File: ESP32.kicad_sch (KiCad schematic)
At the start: 5 parts, among them U1 ESP32-S3-WROOM-1

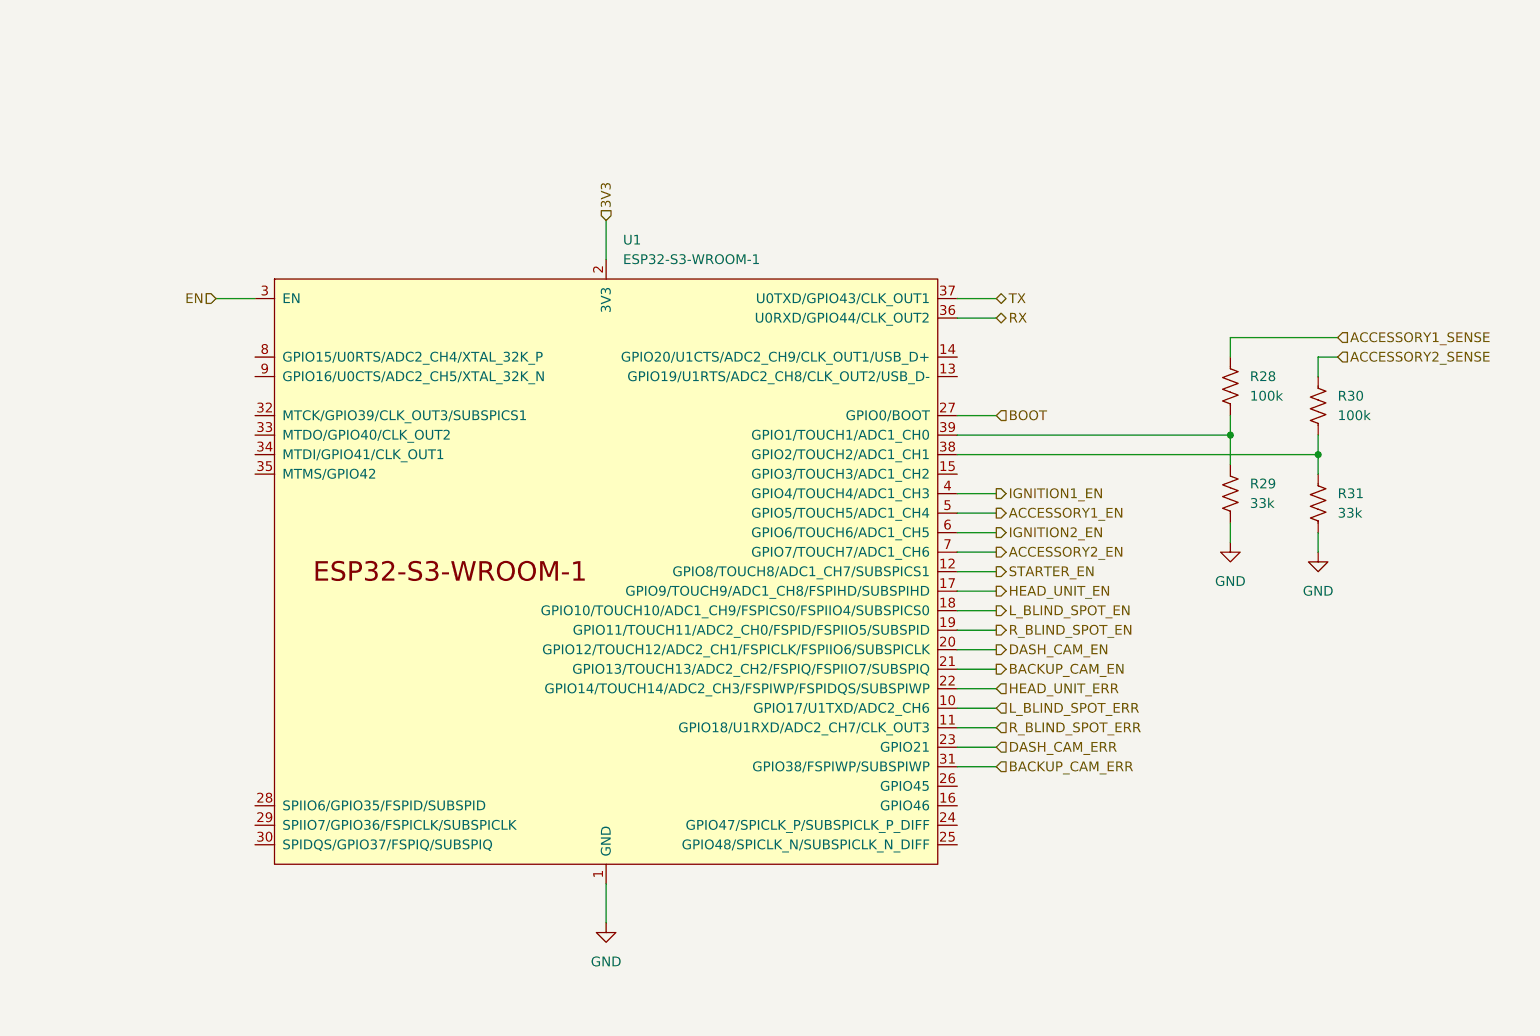
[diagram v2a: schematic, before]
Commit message: switch Ignition page to use load drivers rather than discrete FETs
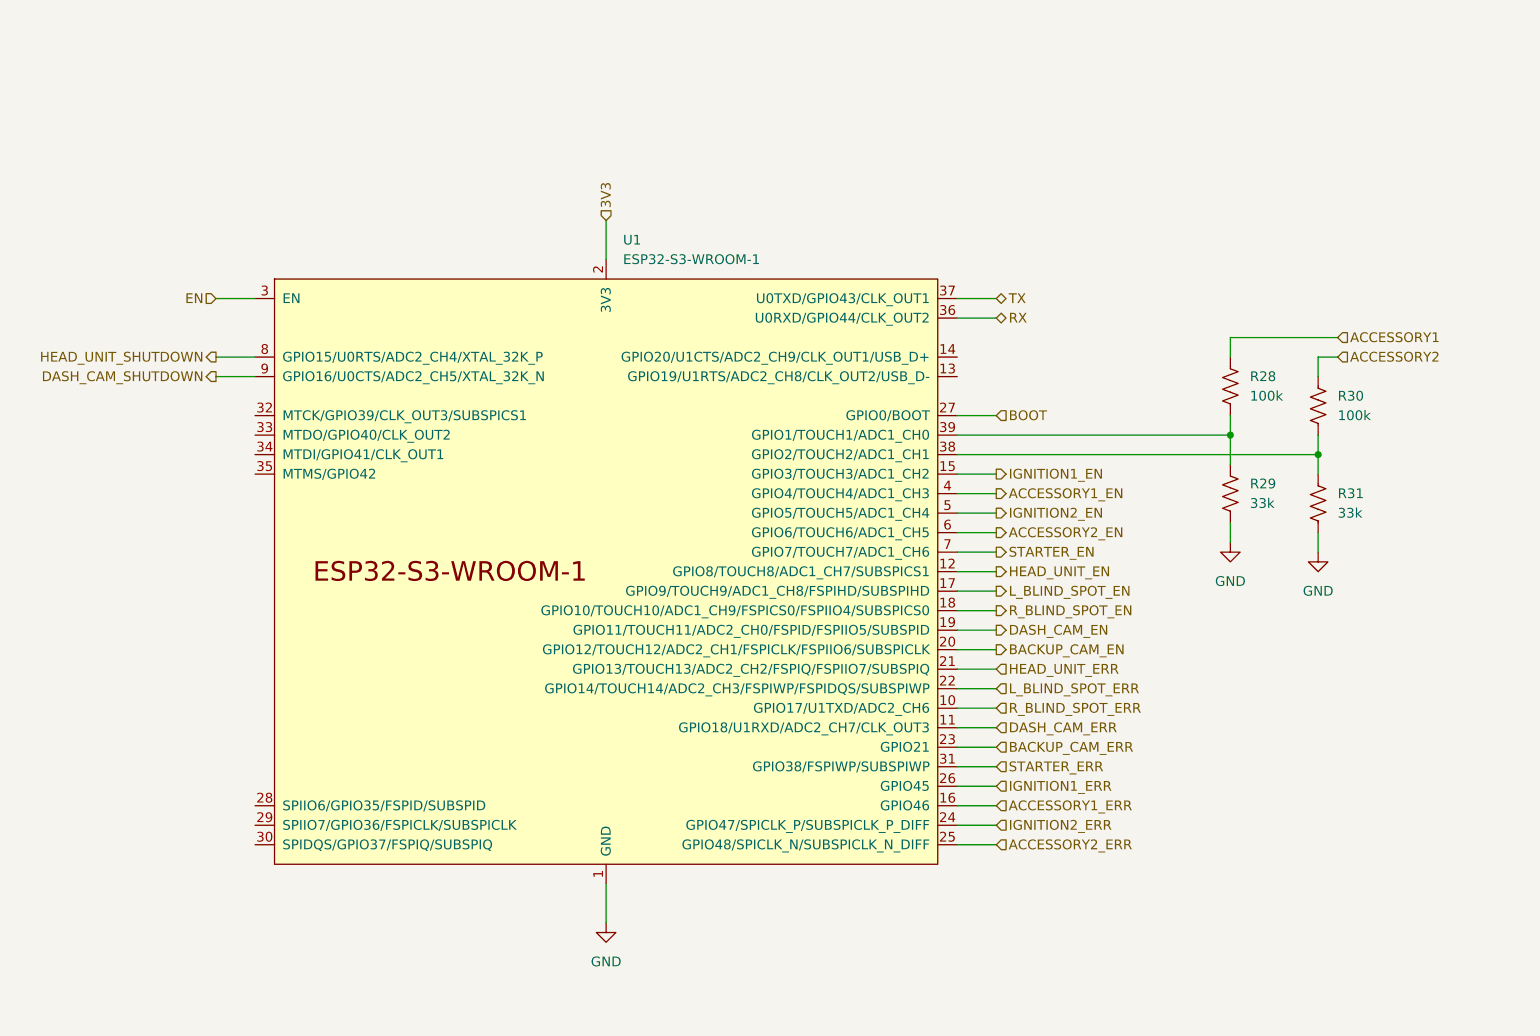
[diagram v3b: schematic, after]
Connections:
- net ACCESSORY1_EN: now also U1.4 (GPIO4/TOUCH4/ADC1_CH3); no longer U1.5 (GPIO5/TOUCH5/ADC1_CH4)
- net ACCESSORY2_EN: now also U1.6 (GPIO6/TOUCH6/ADC1_CH5); no longer U1.7 (GPIO7/TOUCH7/ADC1_CH6)
- net BACKUP_CAM_EN: now also U1.20 (GPIO12/TOUCH12/ADC2_CH1/FSPICLK/FSPIIO6/SUBSPICLK); no longer U1.21 (GPIO13/TOUCH13/ADC2_CH2/FSPIQ/FSPIIO7/SUBSPIQ)
- net BACKUP_CAM_ERR: now also U1.23 (GPIO21); no longer U1.31 (GPIO38/FSPIWP/SUBSPIWP)
- net DASH_CAM_EN: now also U1.19 (GPIO11/TOUCH11/ADC2_CH0/FSPID/FSPIIO5/SUBSPID); no longer U1.20 (GPIO12/TOUCH12/ADC2_CH1/FSPICLK/FSPIIO6/SUBSPICLK)
- net DASH_CAM_ERR: now also U1.11 (GPIO18/U1RXD/ADC2_CH7/CLK_OUT3); no longer U1.23 (GPIO21)
- net HEAD_UNIT_EN: now also U1.12 (GPIO8/TOUCH8/ADC1_CH7/SUBSPICS1); no longer U1.17 (GPIO9/TOUCH9/ADC1_CH8/FSPIHD/SUBSPIHD)
- net HEAD_UNIT_ERR: now also U1.21 (GPIO13/TOUCH13/ADC2_CH2/FSPIQ/FSPIIO7/SUBSPIQ); no longer U1.22 (GPIO14/TOUCH14/ADC2_CH3/FSPIWP/FSPIDQS/SUBSPIWP)
- net IGNITION1_EN: now also U1.15 (GPIO3/TOUCH3/ADC1_CH2); no longer U1.4 (GPIO4/TOUCH4/ADC1_CH3)
- net IGNITION2_EN: now also U1.5 (GPIO5/TOUCH5/ADC1_CH4); no longer U1.6 (GPIO6/TOUCH6/ADC1_CH5)
- net L_BLIND_SPOT_EN: now also U1.17 (GPIO9/TOUCH9/ADC1_CH8/FSPIHD/SUBSPIHD); no longer U1.18 (GPIO10/TOUCH10/ADC1_CH9/FSPICS0/FSPIIO4/SUBSPICS0)
- net L_BLIND_SPOT_ERR: now also U1.22 (GPIO14/TOUCH14/ADC2_CH3/FSPIWP/FSPIDQS/SUBSPIWP); no longer U1.10 (GPIO17/U1TXD/ADC2_CH6)
- net R_BLIND_SPOT_EN: now also U1.18 (GPIO10/TOUCH10/ADC1_CH9/FSPICS0/FSPIIO4/SUBSPICS0); no longer U1.19 (GPIO11/TOUCH11/ADC2_CH0/FSPID/FSPIIO5/SUBSPID)
- net R_BLIND_SPOT_ERR: now also U1.10 (GPIO17/U1TXD/ADC2_CH6); no longer U1.11 (GPIO18/U1RXD/ADC2_CH7/CLK_OUT3)
- net STARTER_EN: now also U1.7 (GPIO7/TOUCH7/ADC1_CH6); no longer U1.12 (GPIO8/TOUCH8/ADC1_CH7/SUBSPICS1)
- net ACCESSORY1_ERR: now reaches U1.16 (GPIO46)
- net IGNITION2_ERR: now reaches U1.24 (GPIO47/SPICLK_P/SUBSPICLK_P_DIFF)
- net ACCESSORY2_ERR: now reaches U1.25 (GPIO48/SPICLK_N/SUBSPICLK_N_DIFF)
- net IGNITION1_ERR: now reaches U1.26 (GPIO45)
- net HEAD_UNIT_SHUTDOWN: now reaches U1.8 (GPIO15/U0RTS/ADC2_CH4/XTAL_32K_P)
- net DASH_CAM_SHUTDOWN: now reaches U1.9 (GPIO16/U0CTS/ADC2_CH5/XTAL_32K_N)
- net ACCESSORY1_SENSE renamed ACCESSORY1
- net ACCESSORY2_SENSE renamed ACCESSORY2
- new net STARTER_ERR: U1.31 (GPIO38/FSPIWP/SUBSPIWP)
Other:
- company: (none) -> J2B

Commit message: fix ERC errors
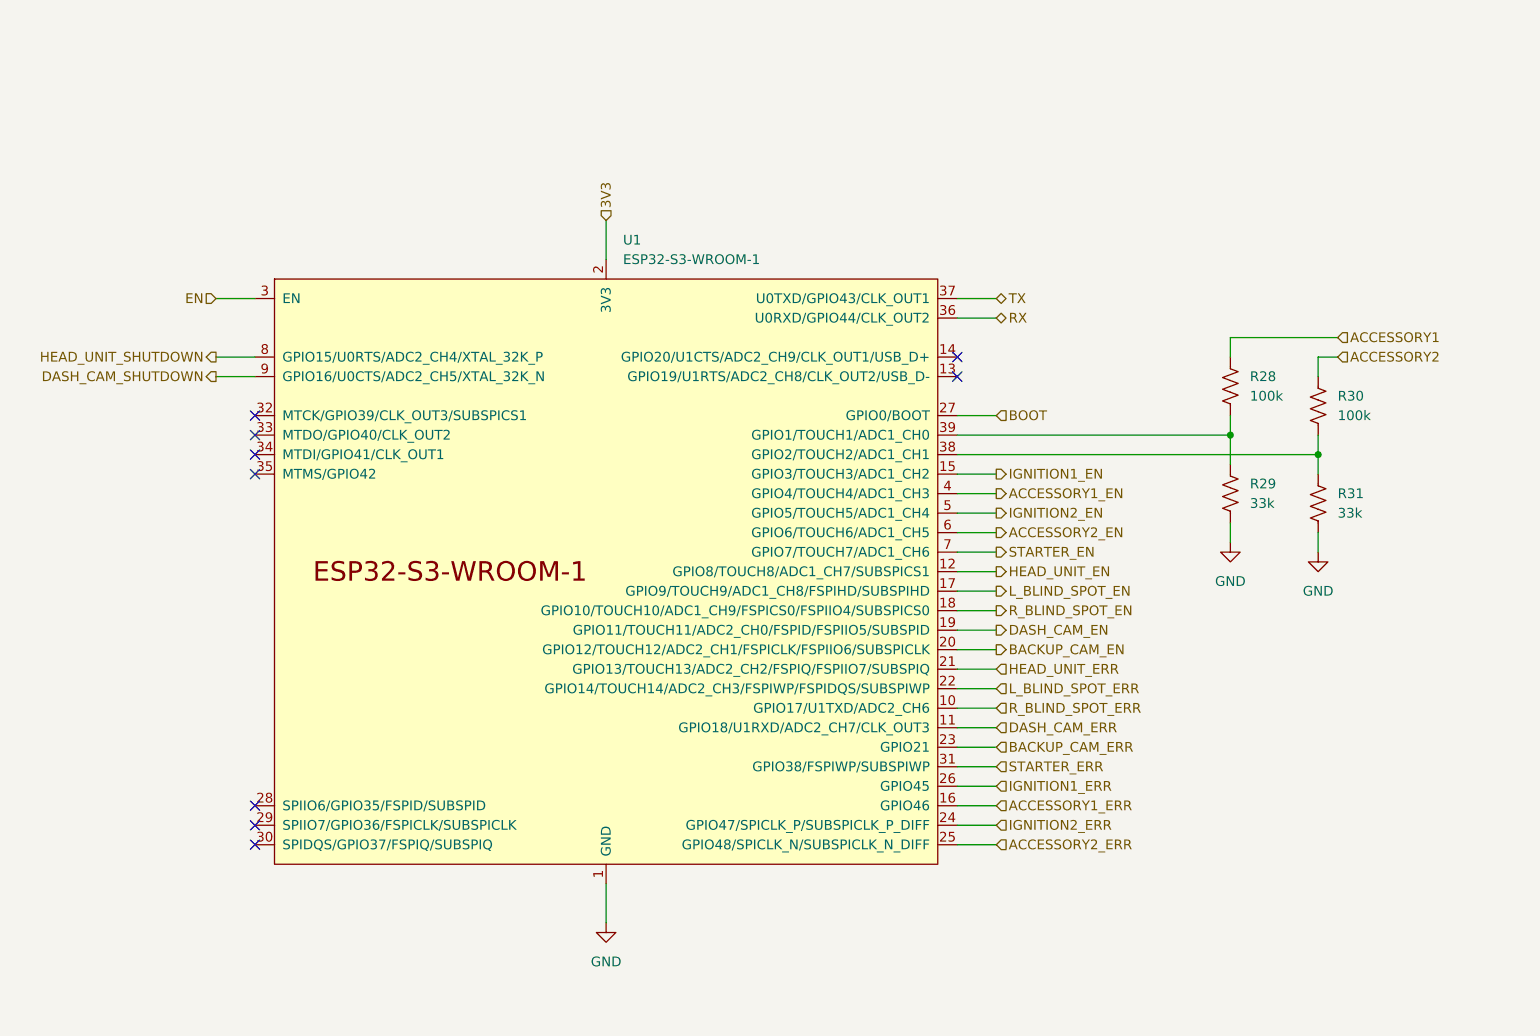
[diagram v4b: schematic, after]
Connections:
- no-connect marks 0 -> 9
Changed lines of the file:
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@@
   (junction (at 228.6 82.55) (diameter 0) (color 0 0 0 0)
   )
+  (no_connect (at 101.6 87.63))
+  (no_connect (at 193.04 72.39))
+  (no_connect (at 193.04 74.93))
+  (no_connect (at 101.6 85.09))
+  (no_connect (at 101.6 82.55))
+  (no_connect (at 101.6 130.81))
+  (no_connect (at 101.6 133.35))
+  (no_connect (at 101.6 80.01))
+  (no_connect (at 101.6 135.89))
   (wire (pts (xy 193.04 107.95) (xy 198.12 107.95))
     (stroke (width 0) (type default))
@@
     (stroke (width 0) (type default))
   )
-  (wire (pts (xy 147.32 54.61) (xy 147.32 59.69))
-    (stroke (width 0) (type default))
-  )
   (wire (pts (xy 228.6 82.55) (xy 228.6 86.36))
     (stroke (width 0) (type default))
@@
     (stroke (width 0) (type default))
   )
+  (wire (pts (xy 147.32 54.61) (xy 147.32 59.69))
+    (stroke (width 0) (type default))
+  )

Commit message: Assigning footprints
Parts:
- R28, R29, R30, R31: footprint (none) -> Resistor_SMD:R_0603_1608Metric
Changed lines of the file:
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@@
       (effects (font (size 1.27 1.27)) (justify left))
     )
-    (property "Footprint" "" (at 229.616 76.454 90)
+    (property "Footprint" "Resistor_SMD:R_0603_1608Metric" (at 229.616 76.454 90)
       (effects (font (size 1.27 1.27)) hide)
     )
@@
       (effects (font (size 1.27 1.27)) (justify left))
     )
-    (property "Footprint" "" (at 241.046 78.994 90)
+    (property "Footprint" "Resistor_SMD:R_0603_1608Metric" (at 241.046 78.994 90)
       (effects (font (size 1.27 1.27)) hide)
     )
@@
       (effects (font (size 1.27 1.27)) (justify left))
     )
-    (property "Footprint" "" (at 229.616 90.424 90)
+    (property "Footprint" "Resistor_SMD:R_0603_1608Metric" (at 229.616 90.424 90)
       (effects (font (size 1.27 1.27)) hide)
     )
@@
       (effects (font (size 1.27 1.27)) (justify left))
     )
-    (property "Footprint" "" (at 241.046 91.694 90)
+    (property "Footprint" "Resistor_SMD:R_0603_1608Metric" (at 241.046 91.694 90)
       (effects (font (size 1.27 1.27)) hide)
     )

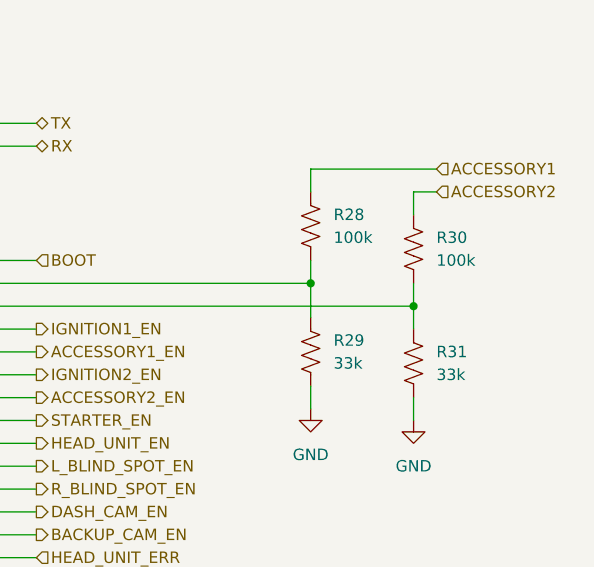
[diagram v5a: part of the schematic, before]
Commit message: finished assigning footprints and started PCB layout
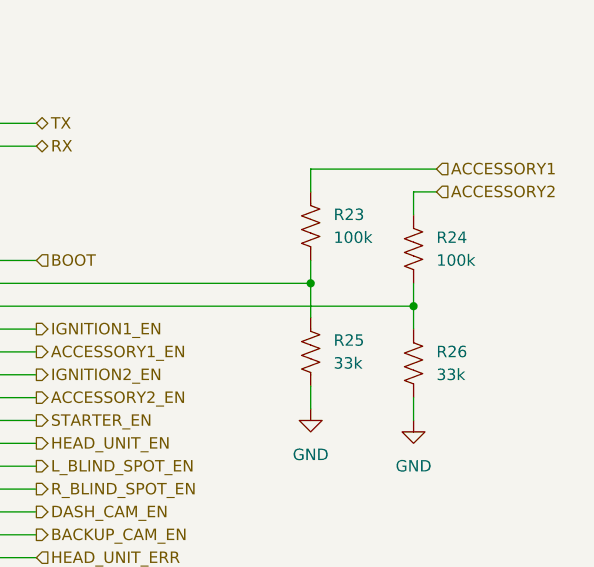
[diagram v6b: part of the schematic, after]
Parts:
- renumbered R28 to R23, R30 to R24, R29 to R25, R31 to R26
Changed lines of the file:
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@@
   (symbol (lib_id "Device:R_US") (at 228.6 76.2 0) (unit 1)
     (in_bom yes) (on_board yes) (dnp no) (fields_autoplaced)
-    (property "Reference" "R28" (at 231.14 74.93 0)
+    (property "Reference" "R23" (at 231.14 74.93 0)
       (effects (font (size 1.27 1.27)) (justify left))
     )
@@
       (project "control-module-pcb"
         (path "/4c946e98-79c2-4a2d-bd7f-2a33db8d8c91/e59499ee-e888-4aa2-b1ef-f071d9b1365d"
-          (reference "R28") (unit 1)
+          (reference "R23") (unit 1)
         )
       )
@@
   (symbol (lib_id "Device:R_US") (at 240.03 78.74 0) (unit 1)
     (in_bom yes) (on_board yes) (dnp no) (fields_autoplaced)
-    (property "Reference" "R30" (at 242.57 77.47 0)
+    (property "Reference" "R24" (at 242.57 77.47 0)
       (effects (font (size 1.27 1.27)) (justify left))
     )
@@
       (project "control-module-pcb"
         (path "/4c946e98-79c2-4a2d-bd7f-2a33db8d8c91/e59499ee-e888-4aa2-b1ef-f071d9b1365d"
-          (reference "R30") (unit 1)
+          (reference "R24") (unit 1)
         )
       )
@@
   (symbol (lib_id "Device:R_US") (at 228.6 90.17 0) (unit 1)
     (in_bom yes) (on_board yes) (dnp no) (fields_autoplaced)
-    (property "Reference" "R29" (at 231.14 88.9 0)
+    (property "Reference" "R25" (at 231.14 88.9 0)
       (effects (font (size 1.27 1.27)) (justify left))
     )
@@
       (project "control-module-pcb"
         (path "/4c946e98-79c2-4a2d-bd7f-2a33db8d8c91/e59499ee-e888-4aa2-b1ef-f071d9b1365d"
-          (reference "R29") (unit 1)
+          (reference "R25") (unit 1)
         )
       )
@@
   (symbol (lib_id "Device:R_US") (at 240.03 91.44 0) (unit 1)
     (in_bom yes) (on_board yes) (dnp no) (fields_autoplaced)
-    (property "Reference" "R31" (at 242.57 90.17 0)
+    (property "Reference" "R26" (at 242.57 90.17 0)
       (effects (font (size 1.27 1.27)) (justify left))
     )
@@
       (project "control-module-pcb"
         (path "/4c946e98-79c2-4a2d-bd7f-2a33db8d8c91/e59499ee-e888-4aa2-b1ef-f071d9b1365d"
-          (reference "R31") (unit 1)
+          (reference "R26") (unit 1)
         )
       )

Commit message: layout mostly complete
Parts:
- renumbered R25 to R24, R24 to R25
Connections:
- net ACCESSORY1_EN: now also U1.31 (GPIO38/FSPIWP/SUBSPIWP); no longer U1.4 (GPIO4/TOUCH4/ADC1_CH3)
- net ACCESSORY1_ERR: now also U1.30 (SPIDQS/GPIO37/FSPIQ/SUBSPIQ); no longer U1.16 (GPIO46)
- net ACCESSORY2_EN: now also U1.26 (GPIO45); no longer U1.6 (GPIO6/TOUCH6/ADC1_CH5)
- net BACKUP_CAM_EN: now also U1.11 (GPIO18/U1RXD/ADC2_CH7/CLK_OUT3); no longer U1.20 (GPIO12/TOUCH12/ADC2_CH1/FSPICLK/FSPIIO6/SUBSPICLK)
- net BACKUP_CAM_ERR: now also U1.12 (GPIO8/TOUCH8/ADC1_CH7/SUBSPICS1); no longer U1.23 (GPIO21)
- net DASH_CAM_EN: now also U1.15 (GPIO3/TOUCH3/ADC1_CH2); no longer U1.19 (GPIO11/TOUCH11/ADC2_CH0/FSPID/FSPIIO5/SUBSPID)
- net DASH_CAM_ERR: now also U1.16 (GPIO46); no longer U1.11 (GPIO18/U1RXD/ADC2_CH7/CLK_OUT3)
- net HEAD_UNIT_EN: now also U1.21 (GPIO13/TOUCH13/ADC2_CH2/FSPIQ/FSPIIO7/SUBSPIQ); no longer U1.12 (GPIO8/TOUCH8/ADC1_CH7/SUBSPICS1)
- net HEAD_UNIT_ERR: now also U1.22 (GPIO14/TOUCH14/ADC2_CH3/FSPIWP/FSPIDQS/SUBSPIWP); no longer U1.21 (GPIO13/TOUCH13/ADC2_CH2/FSPIQ/FSPIIO7/SUBSPIQ)
- net IGNITION1_EN: now also U1.39 (GPIO1/TOUCH1/ADC1_CH0); no longer U1.15 (GPIO3/TOUCH3/ADC1_CH2)
- net IGNITION1_ERR: now also U1.38 (GPIO2/TOUCH2/ADC1_CH1); no longer U1.26 (GPIO45)
- net IGNITION2_EN: now also U1.29 (SPIIO7/GPIO36/FSPICLK/SUBSPICLK); no longer U1.5 (GPIO5/TOUCH5/ADC1_CH4)
- net IGNITION2_ERR: now also U1.28 (SPIIO6/GPIO35/FSPID/SUBSPID); no longer U1.24 (GPIO47/SPICLK_P/SUBSPICLK_P_DIFF)
- net L_BLIND_SPOT_EN: now also U1.19 (GPIO11/TOUCH11/ADC2_CH0/FSPID/FSPIIO5/SUBSPID); no longer U1.17 (GPIO9/TOUCH9/ADC1_CH8/FSPIHD/SUBSPIHD)
- net L_BLIND_SPOT_ERR: now also U1.20 (GPIO12/TOUCH12/ADC2_CH1/FSPICLK/FSPIIO6/SUBSPICLK); no longer U1.22 (GPIO14/TOUCH14/ADC2_CH3/FSPIWP/FSPIDQS/SUBSPIWP)
- net R_BLIND_SPOT_EN: now also U1.17 (GPIO9/TOUCH9/ADC1_CH8/FSPIHD/SUBSPIHD); no longer U1.18 (GPIO10/TOUCH10/ADC1_CH9/FSPICS0/FSPIIO4/SUBSPICS0)
- net R_BLIND_SPOT_ERR: now also U1.18 (GPIO10/TOUCH10/ADC1_CH9/FSPICS0/FSPIIO4/SUBSPICS0); no longer U1.10 (GPIO17/U1TXD/ADC2_CH6)
- net STARTER_EN: now also U1.24 (GPIO47/SPICLK_P/SUBSPICLK_P_DIFF); no longer U1.7 (GPIO7/TOUCH7/ADC1_CH6)
- net STARTER_ERR: now also U1.23 (GPIO21); no longer U1.31 (GPIO38/FSPIWP/SUBSPIWP)
- net at R23.2, R24.1: now also U1.6 (GPIO6/TOUCH6/ADC1_CH5); no longer U1.39 (GPIO1/TOUCH1/ADC1_CH0)
- net at R25.2, R26.1: now also U1.7 (GPIO7/TOUCH7/ADC1_CH6); no longer U1.38 (GPIO2/TOUCH2/ADC1_CH1)
- no-connect marks 9 -> 7
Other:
- moved on the sheet: R23, R24, R25, R26
